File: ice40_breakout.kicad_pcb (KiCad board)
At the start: 4 copper layers, 80 x 100 mm, 220 parts, among them J1 Conn_01x10, J2 Conn_01x08, J3 Conn_01x06, J4 Conn_01x08, J5 USB_B_Micro, J6 7-17 V IN, Q1 DMP3099L-7, Q2 Q_NMOS_GSD, SW1 SW_Push, SW2 SW_Push, SW3 SW_Push, SW4 SW_Push, SW5 SW_Push, SW6 SW_Push, SW7 JS202011SCQN, SW8 JS202011SCQN, SW9 JS202011SCQN, U1 ICE40HX4K-TQ144, U10 MAX40200AUK, U11 SN74LVC2T45DCUR, U12 TPS562201, U13 SN74AXC4T245PWR, U14 MIC5365-3.3YC5, U15 MAX40200AUK, U16 SN74LVC2T45DCUR, U17 SN74LVC2T45DCUR, U18 SN74LVC2T45DCUR, U19 SN74LVC2T45DCUR, U2 IS61WV5128EDBLL-10TLI, U3 93LCxxBT-I_OT, U4 FT2232H, U5 IS25LP080D, U6 TLV62568APDRLR, U7 TLV62568APDRLR, U8 TXS0108EPW, U9 TXS0108EPW, Y1 ECS-3225S33-120-FN-TR, Y2 ECS-3225S33-500-FN-TR

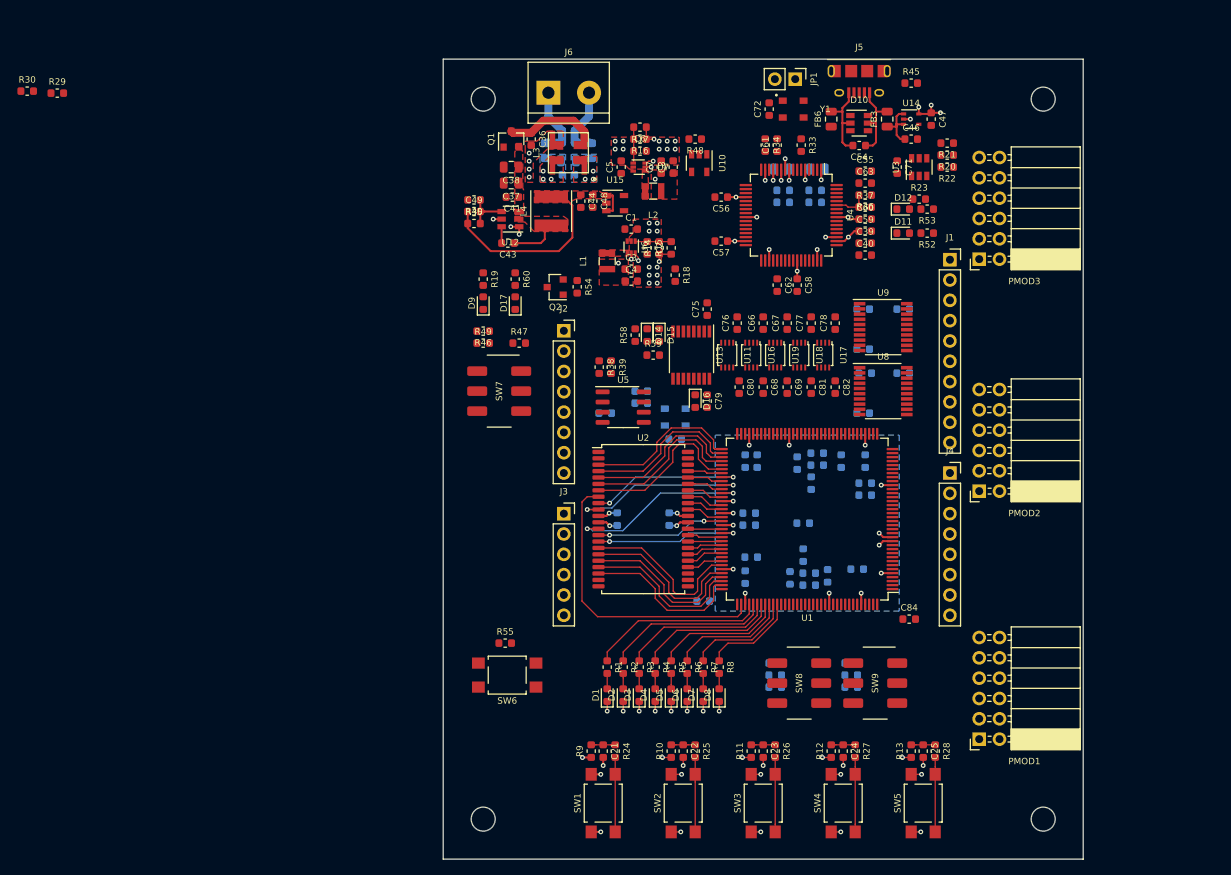
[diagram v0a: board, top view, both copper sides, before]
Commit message: Continued with routing and added ADC
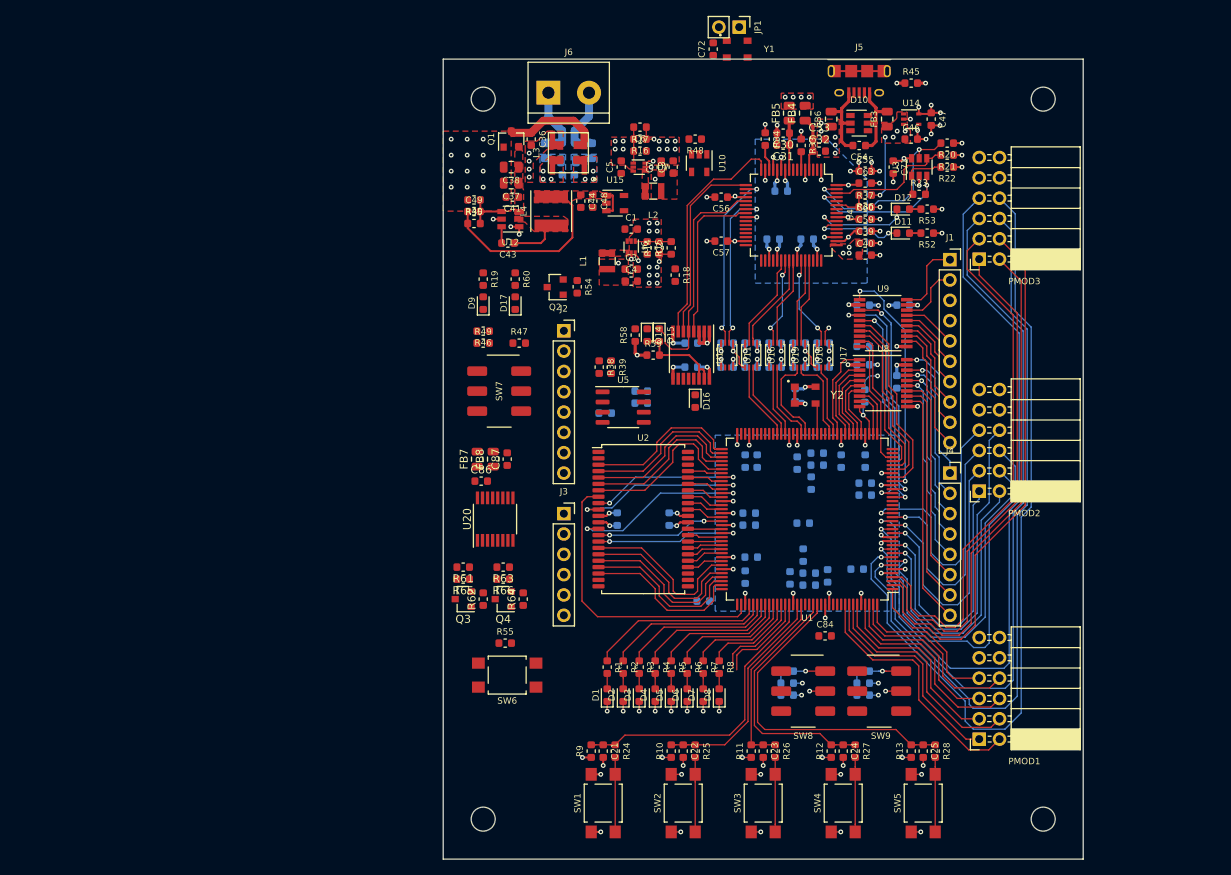
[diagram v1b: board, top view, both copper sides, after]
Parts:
- removed R29, R30: 4,7k, Resistor_SMD:R_0603_1608Metric
- added C86: 100nF, Capacitor_SMD:C_0603_1608Metric, F.Cu at (104.8, 92.8)
- added C87: 10 uF 6,3 V, Capacitor_SMD:C_0603_1608Metric, F.Cu at (108.0, 90.0)
- added FB7: 330 Ohm, Resistor_SMD:R_0805_2012Metric, F.Cu at (104.2, 90.0)
- added FB8: 330 Ohm, Resistor_SMD:R_0805_2012Metric, F.Cu at (106.2, 90.0)
- added Q3: Q_NMOS_GSD, Package_TO_SOT_SMD:SOT-23, F.Cu at (102.5, 107.5)
- added Q4: Q_NMOS_GSD, Package_TO_SOT_SMD:SOT-23, F.Cu at (107.5, 107.5)
- added R61: 4,7k, Resistor_SMD:R_0603_1608Metric, F.Cu at (102.5, 103.5)
- added R62: 4,7k, Resistor_SMD:R_0603_1608Metric, F.Cu at (105.0, 107.5)
- added R63: 4,7k, Resistor_SMD:R_0603_1608Metric, F.Cu at (107.5, 103.5)
- added R64: 4,7k, Resistor_SMD:R_0603_1608Metric, F.Cu at (110.0, 107.5)
- added R65: 0, Resistor_SMD:R_0603_1608Metric, F.Cu at (102.5, 105.0)
- added R66: 0, Resistor_SMD:R_0603_1608Metric, F.Cu at (107.5, 105.0)
- added U20: MAX11614, Package_SO:QSOP-16_3.9x4.9mm_P0.635mm, F.Cu at (106.5, 97.5)
- C30, C31, C32, C33, FB4, FB5, Y2: moved to F.Cu
- C58, C61, C62, C66, C67, C68, C69, C75, C76, C77, C78, C79, C80, C81, C82: moved to B.Cu
- moved Y2 16.5 mm to (145.2, 82.0)
- moved C73 16.0 mm to (144.0, 82.0), turned to 90 degrees
- moved C84 10.7 mm to (147.7, 112.1)
- moved C72 10.3 mm to (133.8, 38.8)
- moved Y1 10.3 mm to (136.8, 38.8)
- moved JP1 9.55 mm to (137.0, 36.0)
- moved C30 8.65 mm to (142.5, 49.2)
- moved C33 7.92 mm to (147.0, 50.0)
- moved FB4 7.16 mm to (145.2, 46.8), turned to 90 degrees
- moved FB5 7.07 mm to (143.2, 46.8), turned to 90 degrees
- moved C58 5.88 mm to (145.5, 62.5), turned to 0 degrees
- moved C61 5.77 mm to (142.2, 56.5), turned to 0 degrees
- moved C62 5.77 mm to (141.2, 62.5), turned to 180 degrees
- moved C31 5.65 mm to (142.5, 50.8)
- moved C32 4.93 mm to (147.0, 51.5)
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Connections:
- J3 pad 1: (no net) -> /Header/INO_A0
- J3 pad 2: (no net) -> /Header/INO_A1
- J3 pad 3: (no net) -> /Header/INO_A2
- J3 pad 4: (no net) -> /Header/INO_A3
- J3 pad 5: (no net) -> /Header/INO_A4
- J3 pad 6: (no net) -> /Header/INO_A5
- U1 pad 1: /Header/P1_2 -> /Header/P2_3
- U1 pad 10: /Header/P10_2 -> /Header/P1_2
- U1 pad 11: /Header/P1_3 -> /Header/P9_3
- U1 pad 12: /Header/P2_3 -> /Header/P4_2
- U1 pad 120: (no net) -> ADC_SCL_3V3
- U1 pad 121: (no net) -> ADC_SDA_3V3
- U1 pad 137: P2_1 -> P7_1
- U1 pad 138: P3_1 -> P2_1
- U1 pad 139: P4_1 -> P8_1
- U1 pad 141: P7_1 -> P3_1
- U1 pad 142: P8_1 -> P9_1
- U1 pad 143: P9_1 -> P4_1
- U1 pad 15: /Header/P3_3 -> /Header/P7_2
- U1 pad 16: /Header/P4_3 -> /Header/P10_3
- U1 pad 17: /Header/P7_3 -> /Header/P8_2
- U1 pad 18: /Header/P8_3 -> /Header/P3_2
- U1 pad 19: /Header/P9_3 -> /Header/P9_2
- U1 pad 2: /Header/P2_2 -> /Header/P1_3
- U1 pad 20: /Header/P10_3 -> /Header/P10_2
- U1 pad 24: /Header/FPGA_INO_SCL -> /Header/FPGA_INO_SCK
- U1 pad 25: /Header/FPGA_INO_SDA -> /Header/FPGA_INO_MISO
- U1 pad 26: /Header/FPGA_INO_SCK -> /Header/FPGA_INO_SDA
- U1 pad 28: /Header/FPGA_INO_MISO -> /Header/FPGA_INO_SCL
- U1 pad 3: /Header/P3_2 -> /Header/P7_3
- U1 pad 34: /Header/OE0 -> /Header/OE1
- U1 pad 37: /Header/FPGA_INO_D7 -> /Header/FPGA_INO_TX
- U1 pad 38: /Header/FPGA_INO_D6 -> /Header/FPGA_INO_RX
- U1 pad 39: /Header/FPGA_INO_D5 -> /Header/OE0
- U1 pad 4: /Header/P4_2 -> /Header/P8_3
- U1 pad 41: /Header/FPGA_INO_D4 -> /Header/FPGA_INO_D2
- U1 pad 43: /Header/FPGA_INO_D2 -> /Header/FPGA_INO_D4
- U1 pad 44: /Header/FPGA_INO_TX -> /Header/FPGA_INO_D5
- U1 pad 45: /Header/FPGA_INO_RX -> /Header/FPGA_INO_D6
- U1 pad 47: /Header/OE1 -> /Header/FPGA_INO_D7
- U1 pad 48: TXD -> ~DTR~
- U1 pad 49: RXD -> ~DCD~
- U1 pad 55: ~RTS~ -> ~DSR~
- U1 pad 60: ~DTR~ -> RXD
- U1 pad 61: ~DSR~ -> ~RTS~
- U1 pad 62: ~DCD~ -> TXD
- U1 pad 7: /Header/P7_2 -> /Header/P3_3
- U1 pad 8: /Header/P8_2 -> /Header/P2_2
- U1 pad 9: /Header/P9_2 -> /Header/P4_3
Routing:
- net /Header/P4_3: track 0.00 -> 102.3 mm, vias 0 -> 1
- net /Header/P3_3: track 0.00 -> 92.5 mm, vias 0 -> 1
- net /Header/P10_3: track 0.00 -> 92.4 mm, vias 0 -> 1
- net /Header/P9_3: track 0.00 -> 91.4 mm, vias 0 -> 1
- net GND: track 61.9 -> 129.6 mm, vias 71 -> 130
- net /Header/P2_3: track 0.00 -> 67.2 mm
- net /Header/P8_3: track 0.00 -> 66.6 mm
- net /Header/P1_3: track 0.00 -> 64.1 mm
- net /Header/P7_3: track 0.00 -> 63.9 mm
- net /Header/P3_2: track 0.00 -> 53.8 mm, vias 0 -> 1
- net /Header/P4_2: track 0.00 -> 43.7 mm, vias 0 -> 1
- net /Header/P2_2: track 0.00 -> 41.1 mm, vias 0 -> 1
- net /User Interface/SW5: track 3.00 -> 41.2 mm
- net +3V3_FTDI: track 17.6 -> 55.3 mm, vias 8 -> 28
- net +3V3: track 19.9 -> 56.6 mm, vias 10 -> 29
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- added copper zone on B.Cu, net +1V8
- added copper zone on F.Cu, net +1V8
- added copper zone on F.Cu, net +3V3_FTDI
- added copper zone on In1.Cu, net Net-(J5-Pad6)
- added copper zone on F.Cu, net VBUS

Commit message: Changed power isolation to usb power to use an open drain translator for the reset signals. Continued on routing
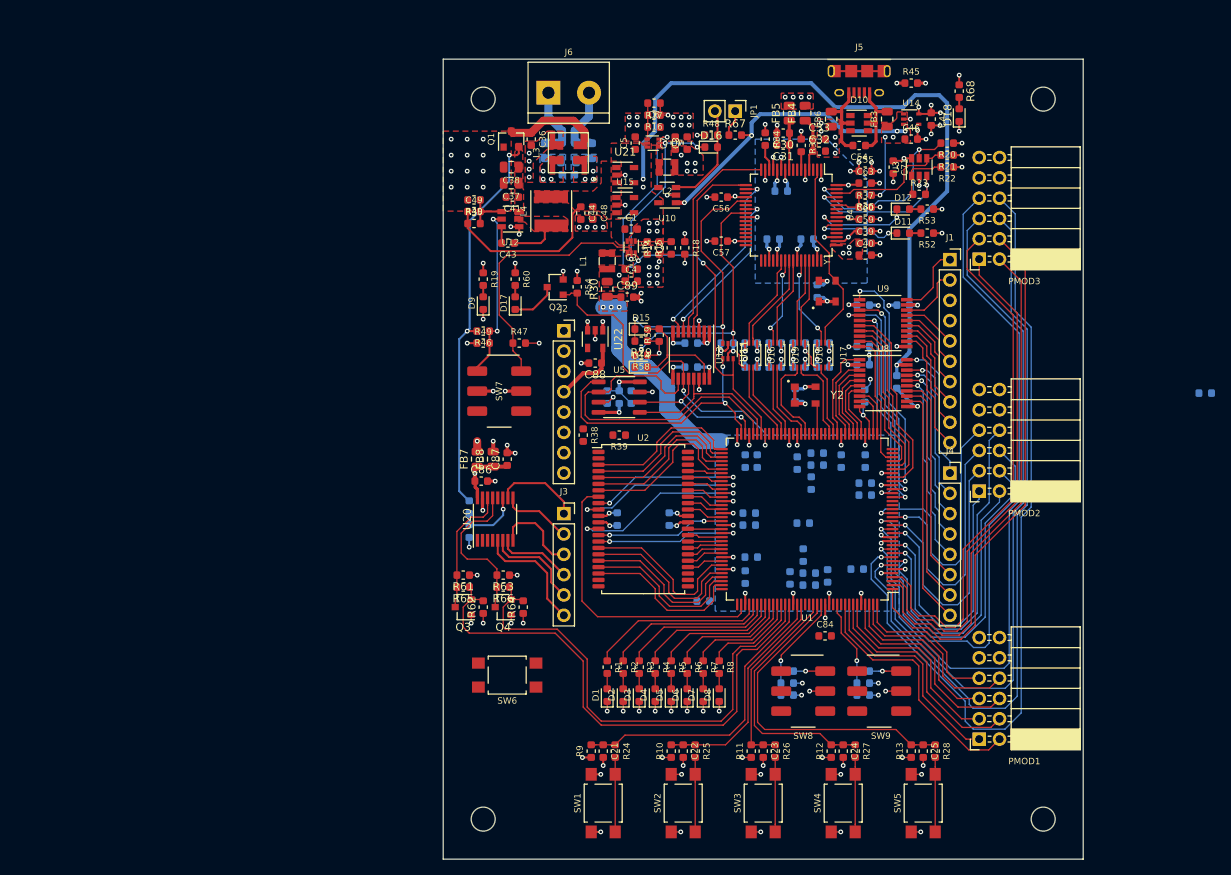
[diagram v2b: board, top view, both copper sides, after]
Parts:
- added C88: 10 uF 6,3 V, Capacitor_SMD:C_0603_1608Metric, F.Cu at (119.0, 78.0)
- added C89: 10 uF 6,3 V, Capacitor_SMD:C_0603_1608Metric, F.Cu at (123.0, 69.8)
- added D18: USB ON LED, LED_SMD:LED_0603_1608Metric, F.Cu at (164.5, 47.0)
- added R29: 10k, Resistor_SMD:R_0603_1608Metric, F.Cu at (124.8, 75.2)
- added R30: 0, Resistor_SMD:R_0805_2012Metric, F.Cu at (120.5, 68.8)
- added R67: 10k, Resistor_SMD:R_0603_1608Metric, F.Cu at (136.5, 49.5)
- added R68: 560, Resistor_SMD:R_0603_1608Metric, F.Cu at (164.5, 44.0)
- added R69: 30k 1%, Resistor_SMD:R_0603_1608Metric, B.Cu at (103.2, 99.0)
- added U21: MAX40200AUK, Package_TO_SOT_SMD:SOT-23-5, F.Cu at (122.8, 54.5)
- added U22: MAX40200AUK, Package_TO_SOT_SMD:SOT-23-5, F.Cu at (119.0, 75.0)
- C72: moved to B.Cu
- JP1: value Jumper_NO_Small -> VBUS_EN
- R55: value 10k -> 270k 1%; moved to B.Cu
- U11: value SN74LVC2T45DCUR -> SN74LVC2G07DCKR; footprint Package_SO:VSSOP-8_2.4x2.1mm_P0.5mm -> Package_TO_SOT_SMD:SOT-363_SC-70-6
- moved C80 59.8 mm to (195.2, 81.8)
- moved C72 32.9 mm to (146.8, 69.0)
- moved Y1 32.3 mm to (148.0, 69.0), turned to 90 degrees
- moved D16 31.8 mm to (133.5, 51.0), turned to 0 degrees
- moved R55 17.6 mm to (103.2, 96.0), turned to 270 degrees
- moved JP1 10.5 mm to (136.5, 46.5)
- moved R38 8.73 mm to (117.5, 87.0)
- moved R39 8.56 mm to (122.0, 87.0), turned to 180 degrees
- moved U10 5.66 mm to (128.0, 57.0), turned to 180 degrees
- moved D14 4.07 mm to (124.8, 78.5), turned to 0 degrees
- moved R18 3.61 mm to (130.2, 63.6)
- moved C5 3.47 mm to (124.0, 50.5)
- moved C6 3.47 mm to (126.3, 45.5)
- moved C7 3.47 mm to (129.0, 50.5)
- moved C8 3.47 mm to (130.5, 50.5)
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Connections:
- C2 pad 1: +1V2 -> /power/1V2_REG
- C3 pad 1: +1V2 -> /power/1V2_REG
- C37 pad 1: /power/V_IN_PROTECTED -> V_IN_PROTECTED
- C38 pad 1: /power/V_IN_PROTECTED -> V_IN_PROTECTED
- C4 pad 1: +1V2 -> /power/1V2_REG
- C41 pad 1: /power/V_IN_PROTECTED -> V_IN_PROTECTED
- D16 pad 1: Net-(D16-Pad1) -> /power/EN_LOW_VOLTAGE
- D16 pad 2: CRESET_B -> Net-(D16-Pad2)
- J2 pad 2: (no net) -> +5V
- J2 pad 4: (no net) -> /Header/INO_3V3
- J2 pad 5: (no net) -> +5V
- JP1 pad 1: VBUS -> Net-(JP1-Pad1)
- JP1 pad 2: Net-(JP1-Pad2) -> Net-(D16-Pad2)
- L1 pad 2: +1V2 -> /power/1V2_REG
- Q1 pad 2: /power/V_IN_PROTECTED -> V_IN_PROTECTED
- R14 pad 1: +1V2 -> /power/1V2_REG
- R18 pad 2: PG -> CRESET_B
- R46 pad 2: /power/V_IN_PROTECTED -> V_IN_PROTECTED
- R48 pad 2: Net-(JP1-Pad2) -> Net-(D16-Pad2)
- R55 pad 1: +3V3 -> V_IN_PROTECTED
- R55 pad 2: CRESET_B -> Net-(R55-Pad2)
- R61 pad 1: +5V -> /Header/ADC_VCC
- R63 pad 1: +5V -> /Header/ADC_VCC
- U10 pad 3: Net-(JP1-Pad2) -> Net-(D16-Pad2)
- U11 pad 1: +3V3_FTDI -> /USB Programmer/FTDI_CRESET_B
- U11 pad 2: /USB Programmer/FTDI_CDONE -> GND
- U11 pad 3: /USB Programmer/FTDI_MISO -> /USB Programmer/FTDI_SS
- U11 pad 4: GND -> /USB Programmer/SS
- U11 pad 5: GND -> +3V3_FTDI
- U11 pad 6: /USB Programmer/MISO -> CRESET_B
- U12 pad 3: /power/V_IN_PROTECTED -> V_IN_PROTECTED
- U13 pad 10: /USB Programmer/SCK -> /USB Programmer/MISO
- U13 pad 11: /USB Programmer/MOSI -> CDONE
- U13 pad 12: /USB Programmer/SS -> /USB Programmer/SCK
- U13 pad 13: Net-(D16-Pad1) -> /USB Programmer/MOSI
- U13 pad 14: Net-(D14-Pad2) -> GND
- U13 pad 3: +3V3_FTDI -> GND
- U13 pad 4: /USB Programmer/FTDI_CRESET_B -> /USB Programmer/FTDI_MOSI
- U13 pad 5: /USB Programmer/FTDI_SS -> /USB Programmer/FTDI_SCK
- U13 pad 6: /USB Programmer/FTDI_MOSI -> /USB Programmer/FTDI_CDONE
- U13 pad 7: /USB Programmer/FTDI_SCK -> /USB Programmer/FTDI_MISO
- U20 pad 11: (no net) -> Net-(R55-Pad2)
- U6 pad 6: PG -> CRESET_B
- U7 pad 6: PG -> CRESET_B
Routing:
- net +5V: track 4.95 -> 147.9 mm, vias 2 -> 6
- net CRESET_B: track 0.00 -> 61.1 mm, vias 0 -> 4
- net ADC_SDA_3V3: track 11.7 -> 67.4 mm
- net /power/EN_LOW_VOLTAGE: track 1.50 -> 55.9 mm, vias 2 -> 3
- net ADC_SCL_3V3: track 11.5 -> 61.5 mm
- net V_IN_PROTECTED: track 0.00 -> 49.6 mm, vias 0 -> 2
- net /USB Programmer/MISO: track 0.00 -> 44.0 mm
- net CDONE: track 0.00 -> 42.9 mm, vias 0 -> 2
- net VBUS: track 8.58 -> 44.9 mm, vias 5 -> 7
- net /USB Programmer/SS: track 0.00 -> 35.6 mm, vias 0 -> 2
- net GND: track 129.6 -> 163.1 mm, vias 130 -> 156
- net /USB Programmer/12_MHZ: track 2.04 -> 24.1 mm, vias 1 -> 0
- net /USB Programmer/MOSI: track 0.00 -> 21.0 mm
- net /power/EN_HIGH_VOLTAGE: track 1.05 -> 21.9 mm, vias 1 -> 2
- net +1V2: track 13.7 -> 33.8 mm, vias 6 -> 7
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- added copper zone on F.Cu, net +5V
- added copper zone on In2.Cu, net /Header/ADC_VCC
- added copper zone on F.Cu, net /power/1V2_REG
- added copper zone on F.Cu, net V_IN_PROTECTED
- removed copper zone on F.Cu, net /power/V_IN_PROTECTED

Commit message: Routing mostly done
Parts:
- removed C80: 100nF, Capacitor_SMD:C_0603_1608Metric
- moved R39 12.0 mm to (133.8, 84.8)
- moved C65 9.51 mm to (138.8, 80.8), turned to 0 degrees
- moved R38 4.28 mm to (121.8, 86.5), turned to 180 degrees
- moved C15 4.01 mm to (149.0, 108.5)
- moved C11 3.78 mm to (143.8, 86.8), turned to 180 degrees
- moved D13 3.75 mm to (134.8, 104.8), turned to 90 degrees
- moved C64 3.51 mm to (137.5, 86.8), turned to 0 degrees
- moved R41 3.36 mm to (143.8, 90.5)
- moved R67 3.35 mm to (133.5, 48.0), turned to 180 degrees
- moved R42 2.85 mm to (143.2, 104.2)
- moved C16 2.33 mm to (142.0, 106.8), turned to 180 degrees
- moved C12 1.25 mm to (149.0, 89.2), turned to 180 degrees
- moved C13 1.25 mm to (152.8, 91.8)
- moved C17 1.25 mm to (152.0, 89.2), turned to 180 degrees
- moved C20 1.25 mm to (152.8, 93.2)
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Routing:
- net CRESET_B: track 61.1 -> 123.1 mm, vias 4 -> 5
- net +5V: track 147.9 -> 105.9 mm, vias 6 -> 7
- net VBUS: track 44.9 -> 10.4 mm, vias 7 -> 8
- net GND: track 163.1 -> 186.7 mm, vias 156 -> 170
- net /USB Programmer/D_P: track 0.00 -> 22.7 mm, vias 0 -> 2
- net /USB Programmer/D_N: track 0.00 -> 21.1 mm, vias 0 -> 2
- net +3V3: track 75.0 -> 95.5 mm, vias 44 -> 51
- net /power/VCCPLL_1: track 0.00 -> 6.36 mm, vias 0 -> 1
- net /power/VCCPLL_0: track 0.00 -> 6.11 mm, vias 0 -> 1
- net /USB Programmer/FTDI_MISO: track 23.8 -> 29.3 mm
- net /power/GNDPLL_1: track 0.00 -> 4.89 mm, vias 0 -> 1
- net /power/GNDPLL_0: track 0.00 -> 4.64 mm, vias 0 -> 1
- net /USB Programmer/FTDI_CDONE: track 20.6 -> 24.8 mm
- net +1V2: track 33.8 -> 37.1 mm
- net /USB Programmer/~FTDI_DTR~: track 11.5 -> 14.8 mm
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- added copper zone on In2.Cu, net VBUS
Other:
- outline, holes or cut-outs redrawn
